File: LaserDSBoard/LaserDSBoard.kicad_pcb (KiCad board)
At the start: 4 copper layers, 139.5 x 77 mm, 728 parts, among them J1 JTAG, J10 D SWITCH, J11 LASER, J12 Y VREF, J13 X VREF, J14 Y1 MOTOR, J15 X MOTOR, J16 Y2 MOTOR, J17 Y VREF, J2 USB, J3 POWER IN, J4 LASER P, J5 X LIMIT1, J6 WATER FLOW, J7 X LIMIT2, J8 Y LIMIT1, J9 Y LIMIT2, SW1 DHT-1163S, SW2 SSSS213202, U1 LD1117S, U10 TLP2355, U11 ADUM1250, U12 TLP2355, U13 TLP2355, U14 TLP2355, U15 TLP2355, U16 TLP2355, U17 TLP2355, U18 TLP2355, U19 MCP3425, U2 LD1117S, U20 A4982SLPTR, U21 A4982SLPTR, U22 TLP2355, U23 TPL0401A, U24 TPL0401B, U25 A4982SLPTR, U3 STM32F20XR, U4 LD1117S, U5 ADUM1250, U6 TLP2355, U7 TLP2355, U8 TLP2355, U9 TLP2355, X1 7B-25.000MAAJ-T, X2 9HT10-32.768KDZY-T

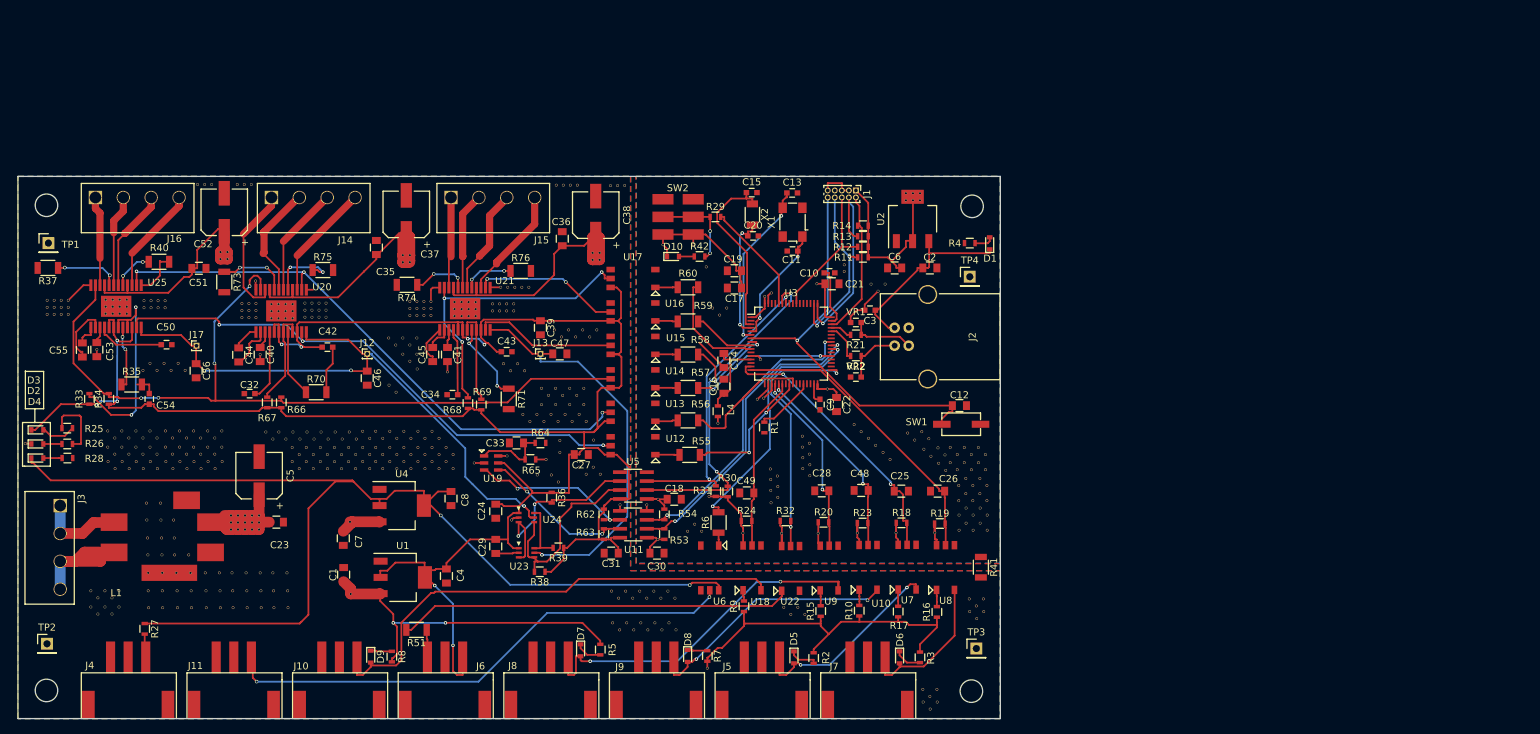
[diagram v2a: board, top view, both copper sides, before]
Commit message: Ver2.0.0
[schematic]
・デジタルポテンショメータ　MCP4461に戻す
・フォトカプラ ENの経路(U14,U17,U29)
TLP2355→TLP291に変更

[AW]
・回路図変更に伴うAW変更
・モータドライバ回りビア増加
・SW2の向きを反転
・部品実装マークをシルクで追加
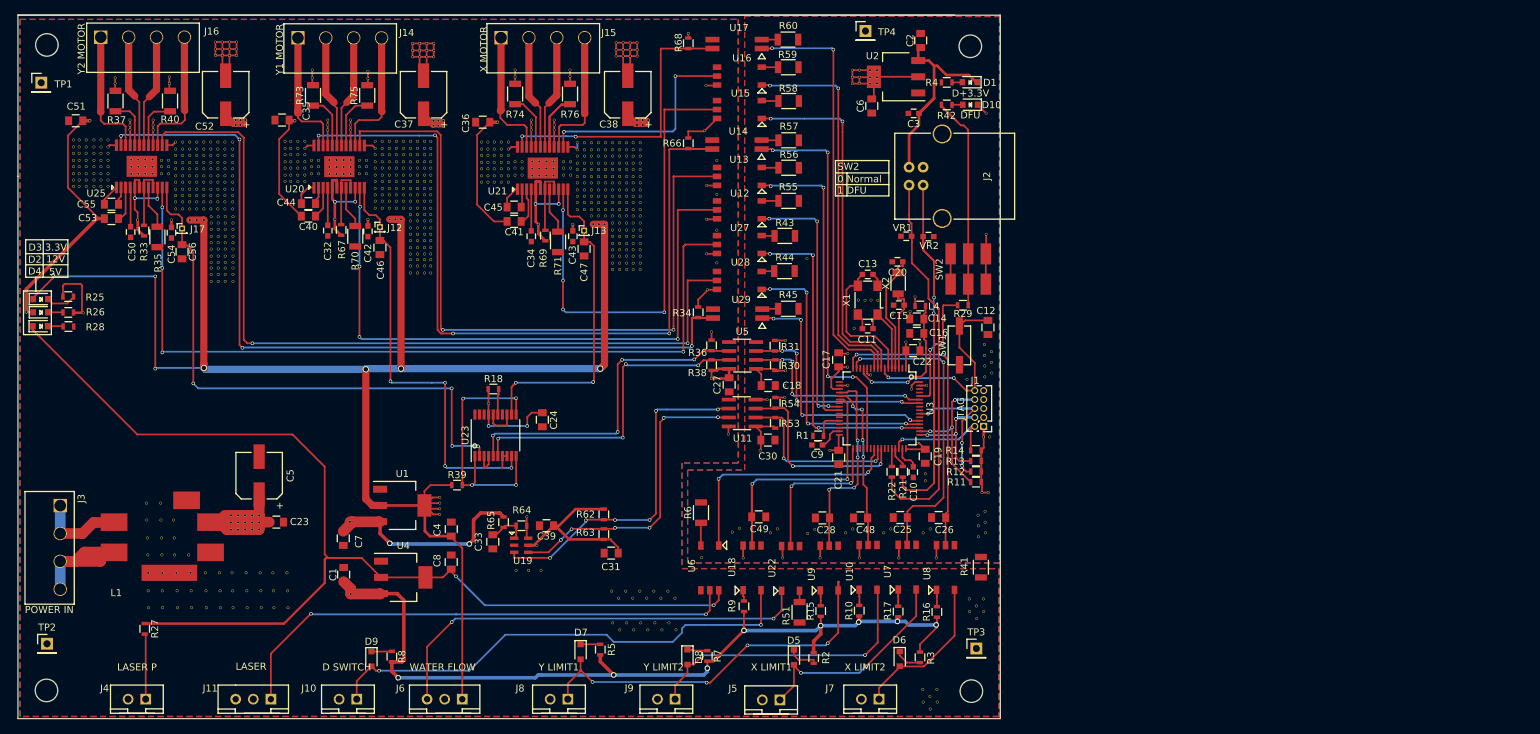
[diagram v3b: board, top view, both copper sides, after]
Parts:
- removed the ? at (201.2, 127.0)
- removed the ? at (243.2, 127.2)
- removed the ? at (244.2, 128.2)
- removed the ? at (244.2, 129.8)
- removed the ? at (243.2, 128.8)
- removed the ? at (243.1, 125.8)
- removed the ? at (244.1, 126.8)
- removed the ? at (254.6, 126.5)
- removed the ? at (255.6, 127.5)
- removed the ? at (253.5, 125.5)
- removed the ? at (252.5, 124.5)
- removed the ? at (250.4, 122.5)
- removed the ? at (251.4, 123.5)
- removed the ? at (266.4, 136.6)
- removed the ? at (268.4, 136.6)
- removed the ? at (265.4, 137.6)
- removed the ? at (267.4, 137.6)
- removed the ? at (269.4, 137.6)
- removed the ? at (269.4, 135.4)
- removed the ? at (267.4, 135.4)
- removed the ? at (265.4, 135.4)
- removed the ? at (268.4, 134.4)
- removed the ? at (266.4, 134.4)
- removed the ? at (266.3, 130.2)
- removed the ? at (268.3, 130.2)
- removed the ? at (265.3, 131.2)
- removed the ? at (267.3, 131.2)
- removed the ? at (269.3, 131.2)
- removed the ? at (269.3, 133.3)
- removed the ? at (267.3, 133.3)
- removed the ? at (265.3, 133.3)
- removed the ? at (268.3, 132.3)
- removed the ? at (266.3, 132.3)
- removed the ? at (261.1, 124.5)
- removed the ? at (260.1, 123.5)
- removed the ? at (230.3, 106.0)
- removed the ? at (232.3, 106.0)
- removed the ? at (231.3, 107.0)
- removed the ? at (228.4, 99.2)
- removed the ? at (229.4, 100.2)
- removed the ? at (224.7, 98.8)
- removed the ? at (226.6, 99.2)
- removed the ? at (224.6, 99.2)
- removed the ? at (237.2, 113.3)
- removed the ? at (263.4, 129.1)
- removed the ? at (262.4, 128.1)
- removed the ? at (227.8, 136.7)
- removed the ? at (226.8, 137.7)
- removed the ? at (264.1, 128.0)
- removed the ? at (266.1, 128.0)
- removed the ? at (268.1, 128.0)
- removed the ? at (265.1, 128.9)
- removed the ? at (267.1, 128.9)
- removed the ? at (269.1, 128.9)
- removed the ? at (249.1, 100.8)
- removed the ? at (249.1, 99.8)
- removed the ? at (252.8, 102.6)
- removed the ? at (254.8, 102.6)
- removed the ? at (253.8, 103.6)
- removed the ? at (238.7, 103.8)
- removed the ? at (193.5, 128.8)
- removed the ? at (191.5, 128.8)
- removed the ? at (189.5, 128.8)
- removed the ? at (187.5, 128.8)
- removed the ? at (185.5, 128.8)
- removed the ? at (183.5, 128.8)
- removed the ? at (192.5, 127.8)
- removed the ? at (190.5, 127.8)
- removed the ? at (188.5, 127.8)
- removed the ? at (186.5, 127.8)
- removed the ? at (184.5, 127.8)
- removed the ? at (182.5, 127.8)
- removed the ? at (170.7, 127.8)
- removed the ? at (172.7, 127.8)
- removed the ? at (174.7, 127.8)
- removed the ? at (176.7, 127.8)
- removed the ? at (178.7, 127.8)
- removed the ? at (180.7, 127.8)
- removed the ? at (171.7, 128.8)
- removed the ? at (173.7, 128.8)
- removed the ? at (175.7, 128.8)
- removed the ? at (177.7, 128.8)
- removed the ? at (179.7, 128.8)
- removed the ? at (181.7, 128.8)
- removed the ? at (168.8, 123.6)
- removed the ? at (170.8, 123.6)
- removed the ? at (172.8, 123.6)
- removed the ? at (174.8, 123.6)
- removed the ? at (176.8, 123.6)
- removed the ? at (178.8, 123.6)
- removed the ? at (169.8, 124.6)
- removed the ? at (171.8, 124.6)
- removed the ? at (173.8, 124.6)
- removed the ? at (175.8, 124.6)
- removed the ? at (177.8, 124.6)
- removed the ? at (179.8, 124.6)
- removed the ? at (167.9, 124.6)
- removed the ? at (166.9, 123.6)
- removed the ? at (213.4, 124.8)
- removed the ? at (208.7, 124.8)
- removed the ? at (208.7, 126.5)
- removed the ? at (208.4, 130.7)
- removed the ? at (201.8, 136.1)
- removed the ? at (207.4, 129.7)
- removed the ? at (205.4, 129.7)
- removed the ? at (211.4, 128.6)
- removed the ? at (213.4, 128.6)
- removed the ? at (212.4, 129.6)
- removed the ? at (214.4, 129.6)
- removed the ? at (203.7, 114.9)
- removed the ? at (201.7, 114.9)
- removed the ? at (202.7, 113.9)
- removed the ? at (200.7, 113.9)
- removed the ? at (207.9, 109.1)
- removed the ? at (209.9, 109.1)
- removed the ? at (211.9, 109.1)
- removed the ? at (213.9, 109.1)
- removed the ? at (208.9, 110.1)
- removed the ? at (210.9, 110.1)
- removed the ? at (212.9, 110.1)
- removed the ? at (212.4, 122.1)
- removed the ? at (210.4, 122.1)
- removed the ? at (208.4, 122.1)
- removed the ? at (206.4, 122.1)
- removed the ? at (204.4, 122.1)
- removed the ? at (211.4, 121.1)
- removed the ? at (209.4, 121.1)
- removed the ? at (207.4, 121.1)
- removed the ? at (205.4, 121.1)
- removed the ? at (203.4, 121.1)
- removed the ? at (206.1, 119.7)
- removed the ? at (208.1, 119.7)
- removed the ? at (210.1, 119.7)
- removed the ? at (212.1, 119.7)
- removed the ? at (211.1, 118.4)
- removed the ? at (209.1, 118.4)
- removed the ? at (207.1, 118.4)
- removed the ? at (212.1, 117.4)
- removed the ? at (210.1, 117.4)
- removed the ? at (208.1, 117.4)
- removed the ? at (206.1, 117.4)
- removed the ? at (144.4, 123.5)
- removed the ? at (146.4, 123.5)
- removed the ? at (148.4, 123.5)
- removed the ? at (150.4, 123.5)
- removed the ? at (145.4, 124.5)
- removed the ? at (147.4, 124.5)
- removed the ? at (149.4, 124.5)
- removed the ? at (151.4, 124.5)
- removed the ? at (151.4, 126.8)
- removed the ? at (149.4, 126.8)
- removed the ? at (145.4, 126.8)
- removed the ? at (150.4, 125.8)
- removed the ? at (148.4, 125.8)
- removed the ? at (144.4, 125.8)
- removed the ? at (142.1, 148.4)
- removed the ? at (144.1, 148.4)
- removed the ? at (146.1, 148.4)
- removed the ? at (143.1, 149.4)
- removed the ? at (145.1, 149.4)
- removed the ? at (145.1, 147.2)
- removed the ? at (143.1, 147.2)
- removed the ? at (146.1, 146.2)
- removed the ? at (144.1, 146.2)
- removed the ? at (142.1, 146.2)
- removed the ? at (156.7, 125.8)
- removed the ? at (158.7, 125.8)
- removed the ? at (199.5, 125.0)
- removed the ? at (160.7, 125.8)
- removed the ? at (153.7, 126.8)
- removed the ? at (157.7, 126.8)
- removed the ? at (159.7, 126.8)
- removed the ? at (159.7, 124.5)
- removed the ? at (157.7, 124.5)
- removed the ? at (155.7, 124.5)
- removed the ? at (153.7, 124.5)
- removed the ? at (160.7, 123.5)
- removed the ? at (158.7, 123.5)
- removed the ? at (156.7, 123.5)
- removed the ? at (154.7, 123.5)
- removed the ? at (152.7, 123.5)
- removed the ? at (184.3, 110.2)
- removed the ? at (186.3, 110.2)
- removed the ? at (188.3, 110.2)
- removed the ? at (185.3, 111.2)
- removed the ? at (187.3, 111.2)
- removed the ? at (187.3, 113.5)
- removed the ? at (188.3, 112.5)
- removed the ? at (186.3, 112.5)
- removed the ? at (184.4, 117.0)
- removed the ? at (185.4, 118.0)
- removed the ? at (188.4, 114.7)
- removed the ? at (180.7, 123.5)
- removed the ? at (181.7, 124.5)
- removed the ? at (181.7, 126.8)
- removed the ? at (179.7, 126.8)
- removed the ? at (177.7, 126.8)
- removed the ? at (175.7, 126.8)
- removed the ? at (173.7, 126.8)
- removed the ? at (171.7, 126.8)
- removed the ? at (180.7, 125.8)
- removed the ? at (178.7, 125.8)
- removed the ? at (176.7, 125.8)
- removed the ? at (174.7, 125.8)
- removed the ? at (172.7, 125.8)
- removed the ? at (170.7, 125.8)
- removed the ? at (182.5, 125.8)
- removed the ? at (184.5, 125.8)
- removed the ? at (186.5, 125.8)
- removed the ? at (188.5, 125.8)
- removed the ? at (190.5, 125.8)
- removed the ? at (192.5, 125.8)
- removed the ? at (183.5, 126.8)
- removed the ? at (185.5, 126.8)
- removed the ? at (187.5, 126.8)
- removed the ? at (189.5, 126.8)
- removed the ? at (191.5, 126.8)
- removed the ? at (193.5, 126.8)
- removed the ? at (151.4, 114.8)
- removed the ? at (191.5, 124.5)
- removed the ? at (189.5, 124.5)
- removed the ? at (187.5, 124.5)
- removed the ? at (185.5, 124.5)
- removed the ? at (183.5, 124.5)
- removed the ? at (155.4, 114.8)
- removed the ? at (153.4, 114.8)
- removed the ? at (149.4, 114.8)
- removed the ? at (190.5, 123.5)
- removed the ? at (188.5, 123.5)
- removed the ? at (186.5, 123.5)
- removed the ? at (184.5, 123.5)
- removed the ? at (182.5, 123.5)
- removed the ? at (154.4, 113.8)
- removed the ? at (152.4, 113.8)
- removed the ? at (150.4, 113.8)
- removed the ? at (246.7, 117.5)
- removed the ? at (245.2, 102.5)
- removed the ? at (229.8, 132.8)
- removed the ? at (222.6, 133.2)
- removed the ? at (261.9, 137.9)
- removed the ? at (250.9, 137.9)
- removed the ? at (237.6, 118.8)
- removed the ? at (231.1, 122.3)
- removed the ? at (237.8, 104.3)
- removed the ? at (227.6, 97.0)
- removed the ? at (223.3, 97.0)
- removed the ? at (222.6, 138.8)
- removed the ? at (256.4, 137.9)
- removed the ? at (245.3, 138.0)
- removed the ? at (240.2, 138.0)
- removed the ? at (234.7, 137.9)
- removed the ? at (221.0, 133.9)
- removed the ? at (236.7, 119.0)
- removed the ? at (269.1, 126.8)
- removed the ? at (267.1, 126.8)
- removed the ? at (265.1, 126.8)
- removed the ? at (268.1, 125.8)
- removed the ? at (266.1, 125.8)
- removed the ? at (187.3, 99.5)
- removed the ? at (186.3, 99.5)
- removed the ? at (214.3, 99.2)
- removed the ? at (213.3, 99.2)
- removed the ? at (161.4, 99.0)
- removed the ? at (160.4, 99.0)
- removed the ? at (187.3, 98.5)
- removed the ? at (186.3, 98.5)
- removed the ? at (214.3, 98.2)
- removed the ? at (213.3, 98.2)
- removed the ? at (142.9, 111.9)
- removed the ? at (166.1, 112.6)
- removed the ? at (192.7, 115.0)
- removed the ? at (161.4, 98.0)
- removed the ? at (160.4, 98.0)
- removed the ? at (206.7, 127.5)
- removed the ? at (190.3, 107.0)
- removed the ? at (189.3, 107.0)
- removed the ? at (188.3, 107.0)
- removed the ? at (187.3, 107.0)
- removed the ? at (175.4, 107.3)
- removed the ? at (174.4, 107.3)
- removed the ? at (173.4, 107.3)
- removed the ? at (172.4, 107.3)
- removed the ? at (165.5, 107.3)
- removed the ? at (164.5, 107.3)
- removed the ? at (163.5, 107.3)
- removed the ? at (204.2, 103.0)
- removed the ? at (203.2, 103.0)
- removed the ? at (202.2, 103.0)
- removed the ? at (201.2, 103.0)
- removed the ? at (200.2, 103.0)
- removed the ? at (190.3, 106.0)
- removed the ? at (189.3, 106.0)
- removed the ? at (188.3, 106.0)
- removed the ? at (187.3, 106.0)
- removed the ? at (175.4, 106.3)
- removed the ? at (174.4, 106.3)
- removed the ? at (173.4, 106.3)
- removed the ? at (172.4, 106.3)
- removed the ? at (165.5, 106.3)
- removed the ? at (164.5, 106.3)
- removed the ? at (163.5, 106.3)
- removed the ? at (190.3, 105.0)
- removed the ? at (189.3, 105.0)
- removed the ? at (188.3, 105.0)
- removed the ? at (187.3, 105.0)
- removed the ? at (175.4, 105.3)
- removed the ? at (174.4, 105.3)
- removed the ? at (173.4, 105.3)
- removed the ? at (172.4, 105.3)
- removed the ? at (165.5, 105.3)
- removed the ? at (164.5, 105.3)
- removed the ? at (163.5, 105.3)
- removed the ? at (138.8, 106.9)
- removed the ? at (137.8, 106.9)
- removed the ? at (136.8, 106.9)
- removed the ? at (135.8, 106.9)
- removed the ? at (152.6, 106.0)
- removed the ? at (151.6, 106.0)
- removed the ? at (150.6, 106.0)
- removed the ? at (149.6, 106.0)
- removed the ? at (138.8, 105.9)
- removed the ? at (137.8, 105.9)
- removed the ? at (136.8, 105.9)
- removed the ? at (135.8, 105.9)
- removed the ? at (243.4, 149.5)
- removed the ? at (152.6, 105.0)
- removed the ? at (241.4, 149.5)
- removed the ? at (151.6, 105.0)
- removed the ? at (150.6, 105.0)
- removed the ? at (149.6, 105.0)
- removed the ? at (138.8, 104.9)
- removed the ? at (137.8, 104.9)
- removed the ? at (136.8, 104.9)
- removed the ? at (135.8, 104.9)
- removed the ? at (242.4, 148.5)
- removed the ? at (240.4, 148.5)
- removed the ? at (159.7, 128.8)
- removed the ? at (157.7, 128.8)
- removed the ? at (155.7, 128.8)
- removed the ? at (153.7, 128.8)
- removed the ? at (160.7, 127.8)
- removed the ? at (158.7, 127.8)
- removed the ? at (156.7, 127.8)
- removed the ? at (152.7, 127.8)
- removed the ? at (144.5, 127.8)
- removed the ? at (146.5, 127.8)
- removed the ? at (148.5, 127.8)
- removed the ? at (150.5, 127.8)
- removed the ? at (145.5, 128.8)
- removed the ? at (147.5, 128.8)
- removed the ? at (149.5, 128.8)
- removed the ? at (151.5, 128.8)
- removed the ? at (165.4, 102.2)
- removed the ? at (217.2, 133.9)
- removed the ? at (262.4, 125.8)
- removed the ? at (263.4, 126.8)
- removed the ? at (261.4, 127.0)
- removed the ? at (260.4, 126.0)
- removed the ? at (258.1, 123.8)
- removed the ? at (259.1, 124.8)
- removed the ? at (159.2, 88.5)
- removed the ? at (158.2, 88.5)
- removed the ? at (157.2, 88.5)
- removed the ? at (162.8, 88.5)
- removed the ? at (163.8, 88.5)
- removed the ? at (164.8, 88.5)
- removed the ? at (217.8, 88.6)
- removed the ? at (216.8, 88.6)
- removed the ? at (215.8, 88.6)
- removed the ? at (208.2, 88.5)
- removed the ? at (209.2, 88.5)
- removed the ? at (210.2, 88.5)
- removed the ? at (211.2, 88.5)
- removed the ? at (238.7, 133.7)
- removed the ? at (239.6, 129.8)
- removed the ? at (238.6, 128.8)
- removed the ? at (238.6, 131.9)
- removed the ? at (239.6, 132.9)
- removed the ? at (239.6, 131.3)
- removed the ? at (238.6, 130.3)
- removed C29: 0u1, Capacitors_SMD:C_0805
- removed R19, R20, R23, R24, R32: 1k, Resistors_SMD:R_0603
- removed U24: TPL0401B, mylib:TPL0401
- added ?: , mylib:via, F.Cu at (266.5, 116.1)
- added ?: , mylib:via, F.Cu at (219.1, 84.4)
- added ?: , mylib:via, F.Cu at (180.2, 86.9)
- added ?: , mylib:via, F.Cu at (181.2, 85.9)
- added ?: , mylib:via, F.Cu at (180.2, 85.9)
- added ?: , mylib:via, F.Cu at (153.1, 85.0)
- added ?: , mylib:via, F.Cu at (152.1, 85.0)
- added ?: , mylib:via, F.Cu at (153.1, 86.9)
- added ?: , mylib:via, F.Cu at (152.1, 86.9)
- added ?: , mylib:via, F.Cu at (153.1, 85.9)
- added ?: , mylib:via, F.Cu at (152.1, 85.9)
- added ?: , mylib:via, F.Cu at (173.4, 85.9)
- added ?: , mylib:via, F.Cu at (220.1, 84.4)
- added ?: , mylib:via, F.Cu at (174.4, 85.9)
- added ?: , mylib:via, F.Cu at (173.4, 86.9)
- added ?: , mylib:via, F.Cu at (174.4, 86.9)
- added ?: , mylib:via, F.Cu at (173.4, 85.0)
- added ?: , mylib:via, F.Cu at (174.4, 85.0)
- added ?: , mylib:via, F.Cu at (144.5, 88.7)
- added ?: , mylib:via, F.Cu at (143.5, 88.7)
- added ?: , mylib:via, F.Cu at (142.5, 88.7)
- added ?: , mylib:via, F.Cu at (140.4, 88.7)
- added ?: , mylib:via, F.Cu at (141.4, 88.7)
- added ?: , mylib:via, F.Cu at (219.1, 85.4)
- added ?: , mylib:via, F.Cu at (139.6, 88.7)
- added ?: , mylib:via, F.Cu at (139.6, 82.1)
- added ?: , mylib:via, F.Cu at (139.6, 83.1)
- added ?: , mylib:via, F.Cu at (139.6, 85.0)
- added ?: , mylib:via, F.Cu at (139.6, 84.0)
- added ?: , mylib:via, F.Cu at (139.6, 87.8)
- added ?: , mylib:via, F.Cu at (139.6, 86.9)
- added ?: , mylib:via, F.Cu at (139.6, 85.9)
- added ?: , mylib:via, F.Cu at (140.4, 85.9)
- added ?: , mylib:via, F.Cu at (141.4, 85.9)
- added ?: , mylib:via, F.Cu at (220.1, 85.4)
- added ?: , mylib:via, F.Cu at (140.4, 86.9)
- added ?: , mylib:via, F.Cu at (141.4, 86.9)
- added ?: , mylib:via, F.Cu at (141.4, 87.8)
- added ?: , mylib:via, F.Cu at (140.4, 87.8)
- added ?: , mylib:via, F.Cu at (140.4, 84.0)
- added ?: , mylib:via, F.Cu at (141.4, 84.0)
- added ?: , mylib:via, F.Cu at (140.4, 85.0)
- added ?: , mylib:via, F.Cu at (141.4, 85.0)
- added ?: , mylib:via, F.Cu at (141.4, 83.1)
- added ?: , mylib:via, F.Cu at (140.4, 83.1)
- added ?: , mylib:via, F.Cu at (220.1, 83.5)
- added ?: , mylib:via, F.Cu at (141.4, 82.1)
- added ?: , mylib:via, F.Cu at (140.4, 82.1)
- added ?: , mylib:via, F.Cu at (210.1, 73.1)
- added ?: , mylib:via, F.Cu at (210.1, 72.2)
- added ?: , mylib:via, F.Cu at (202.3, 72.2)
- added ?: , mylib:via, F.Cu at (202.3, 73.2)
- added ?: , mylib:via, F.Cu at (181.4, 73.4)
- added ?: , mylib:via, F.Cu at (181.4, 72.4)
- added ?: , mylib:via, F.Cu at (173.5, 72.2)
- added ?: , mylib:via, F.Cu at (173.5, 73.3)
- added ?: , mylib:via, F.Cu at (219.1, 83.5)
- added ?: , mylib:via, F.Cu at (153.2, 74.1)
- added ?: , mylib:via, F.Cu at (153.2, 73.2)
- added ?: , mylib:via, F.Cu at (145.5, 73.3)
- added ?: , mylib:via, F.Cu at (145.5, 74.1)
- added ?: , mylib:via, F.Cu at (159.7, 70.1)
- added ?: , mylib:via, F.Cu at (160.7, 70.1)
- added ?: , mylib:via, F.Cu at (161.7, 70.1)
- added ?: , mylib:via, F.Cu at (162.7, 70.1)
- added ?: , mylib:via, F.Cu at (162.7, 69.2)
- added ?: , mylib:via, F.Cu at (161.7, 69.2)
- added ?: , mylib:via, F.Cu at (220.1, 82.5)
- added ?: , mylib:via, F.Cu at (160.7, 69.2)
- added ?: , mylib:via, F.Cu at (159.7, 69.2)
- added ?: , mylib:via, F.Cu at (162.7, 68.2)
- added ?: , mylib:via, F.Cu at (161.7, 68.2)
- added ?: , mylib:via, F.Cu at (160.7, 68.2)
- added ?: , mylib:via, F.Cu at (159.7, 68.2)
- added ?: , mylib:via, F.Cu at (187.7, 68.4)
- added ?: , mylib:via, F.Cu at (188.7, 68.4)
- added ?: , mylib:via, F.Cu at (189.7, 68.4)
- added ?: , mylib:via, F.Cu at (190.7, 68.4)
- added ?: , mylib:via, F.Cu at (219.1, 82.5)
- added ?: , mylib:via, F.Cu at (187.7, 69.4)
- added ?: , mylib:via, F.Cu at (188.7, 69.4)
- added ?: , mylib:via, F.Cu at (189.7, 69.4)
- added ?: , mylib:via, F.Cu at (190.7, 69.4)
- added ?: , mylib:via, F.Cu at (190.7, 70.3)
- added ?: , mylib:via, F.Cu at (189.7, 70.3)
- added ?: , mylib:via, F.Cu at (188.7, 70.3)
- added ?: , mylib:via, F.Cu at (187.7, 70.3)
- added ?: , mylib:via, F.Cu at (216.6, 70.2)
- added ?: , mylib:via, F.Cu at (217.6, 70.2)
- added ?: , mylib:via, F.Cu at (219.1, 91.0)
- added ?: , mylib:via, F.Cu at (218.6, 70.2)
- added ?: , mylib:via, F.Cu at (219.6, 70.2)
- added ?: , mylib:via, F.Cu at (219.6, 69.3)
- added ?: , mylib:via, F.Cu at (218.6, 69.3)
- added ?: , mylib:via, F.Cu at (217.6, 69.3)
- added ?: , mylib:via, F.Cu at (216.6, 69.3)
- added ?: , mylib:via, F.Cu at (219.6, 68.3)
- added ?: , mylib:via, F.Cu at (218.6, 68.3)
- added ?: , mylib:via, F.Cu at (217.6, 68.3)
- added ?: , mylib:via, F.Cu at (216.6, 68.3)
- added ?: , mylib:via, F.Cu at (220.1, 91.0)
- added ?: , mylib:via, F.Cu at (182.4, 85.2)
- added ?: , mylib:via, F.Cu at (240.6, 117.0)
- added ?: , mylib:via, F.Cu at (240.6, 118.7)
- added ?: , mylib:via, F.Cu at (234.2, 137.3)
- added ?: , mylib:via, F.Cu at (233.2, 137.8)
- added ?: , mylib:via, F.Cu at (238.6, 137.9)
- added ?: , mylib:via, F.Cu at (239.6, 137.4)
- added ?: , mylib:via, F.Cu at (244.8, 137.5)
- added ?: , mylib:via, F.Cu at (243.8, 138.0)
- added ?: , mylib:via, F.Cu at (249.2, 137.9)
- added ?: , mylib:via, F.Cu at (219.1, 86.3)
- added ?: , mylib:via, F.Cu at (219.1, 92.0)
- added ?: , mylib:via, F.Cu at (250.2, 137.4)
- added ?: , mylib:via, F.Cu at (254.7, 137.9)
- added ?: , mylib:via, F.Cu at (255.7, 137.4)
- added ?: , mylib:via, F.Cu at (261.2, 137.4)
- added ?: , mylib:via, F.Cu at (260.2, 137.9)
- added ?: , mylib:via, F.Cu at (268.1, 136.9)
- added ?: , mylib:via, F.Cu at (269.1, 137.9)
- added ?: , mylib:via, F.Cu at (268.1, 138.5)
- added ?: , mylib:via, F.Cu at (268.1, 135.4)
- added ?: , mylib:via, F.Cu at (269.1, 136.4)
- added ?: , mylib:via, F.Cu at (220.1, 92.0)
- added ?: , mylib:via, F.Cu at (269.1, 134.9)
- added ?: , mylib:via, F.Cu at (259.4, 125.2)
- added ?: , mylib:via, F.Cu at (237.1, 126.2)
- added ?: , mylib:via, F.Cu at (247.0, 126.2)
- added ?: , mylib:via, F.Cu at (249.5, 114.4)
- added ?: , mylib:via, F.Cu at (249.6, 117.0)
- added ?: , mylib:via, F.Cu at (257.8, 110.8)
- added ?: , mylib:via, F.Cu at (260.8, 117.0)
- added ?: , mylib:via, F.Cu at (252.8, 115.5)
- added ?: , mylib:via, F.Cu at (249.6, 112.5)
- added ?: , mylib:via, F.Cu at (220.1, 90.1)
- added ?: , mylib:via, F.Cu at (250.4, 108.9)
- added ?: , mylib:via, F.Cu at (259.8, 110.8)
- added ?: , mylib:via, F.Cu at (258.6, 117.5)
- added ?: , mylib:via, F.Cu at (259.1, 104.4)
- added ?: , mylib:via, F.Cu at (255.9, 106.9)
- added ?: , mylib:via, F.Cu at (258.4, 106.5)
- added ?: , mylib:via, F.Cu at (252.8, 104.9)
- added ?: , mylib:via, F.Cu at (253.8, 104.9)
- added ?: , mylib:via, F.Cu at (268.6, 132.2)
- added ?: , mylib:via, F.Cu at (269.5, 132.2)
- added ?: , mylib:via, F.Cu at (219.1, 90.1)
- added ?: , mylib:via, F.Cu at (269.7, 124.3)
- added ?: , mylib:via, F.Cu at (268.9, 111.2)
- added ?: , mylib:via, F.Cu at (269.9, 112.2)
- added ?: , mylib:via, F.Cu at (269.9, 113.7)
- added ?: , mylib:via, F.Cu at (268.9, 112.7)
- added ?: , mylib:via, F.Cu at (269.0, 115.8)
- added ?: , mylib:via, F.Cu at (270.0, 115.2)
- added ?: , mylib:via, F.Cu at (269.0, 114.2)
- added ?: , mylib:via, F.Cu at (269.2, 95.5)
- added ?: , mylib:via, F.Cu at (252.7, 72.2)
- added ?: , mylib:via, F.Cu at (219.1, 92.9)
- added ?: , mylib:via, F.Cu at (253.7, 72.2)
- added ?: , mylib:via, F.Cu at (253.7, 74.1)
- added ?: , mylib:via, F.Cu at (252.7, 73.2)
- added ?: , mylib:via, F.Cu at (253.7, 73.2)
- added ?: , mylib:via, F.Cu at (252.7, 74.1)
- added ?: , mylib:via, F.Cu at (250.2, 74.1)
- added ?: , mylib:via, F.Cu at (240.7, 110.6)
- added ?: , mylib:via, F.Cu at (240.7, 114.9)
- added ?: , mylib:via, F.Cu at (232.6, 123.9)
- added ?: , mylib:via, F.Cu at (230.2, 116.0)
- added ?: , mylib:via, F.Cu at (220.1, 92.9)
- added ?: , mylib:via, F.Cu at (230.2, 109.4)
- added ?: , mylib:via, F.Cu at (205.4, 139.7)
- added ?: , mylib:via, F.Cu at (226.9, 67.0)
- added ?: , mylib:via, F.Cu at (229.2, 80.8)
- added ?: , mylib:via, F.Cu at (229.4, 74.4)
- added ?: , mylib:via, F.Cu at (229.5, 88.6)
- added ?: , mylib:via, F.Cu at (229.5, 93.4)
- added ?: , mylib:via, F.Cu at (229.6, 103.4)
- added ?: , mylib:via, F.Cu at (229.5, 98.3)
- added ?: , mylib:via, F.Cu at (191.6, 134.5)
- added ?: , mylib:via, F.Cu at (220.1, 100.5)
- added ?: , mylib:via, F.Cu at (191.6, 135.3)
- added ?: , mylib:via, F.Cu at (191.6, 133.7)
- added ?: , mylib:via, F.Cu at (171.0, 79.4)
- added ?: , mylib:via, F.Cu at (141.9, 79.4)
- added ?: , mylib:via, F.Cu at (147.6, 79.3)
- added ?: , mylib:via, F.Cu at (189.4, 91.8)
- added ?: , mylib:via, F.Cu at (188.4, 91.8)
- added ?: , mylib:via, F.Cu at (187.4, 91.8)
- added ?: , mylib:via, F.Cu at (187.4, 92.7)
- added ?: , mylib:via, F.Cu at (188.4, 92.7)
- added ?: , mylib:via, F.Cu at (219.1, 100.5)
- added ?: , mylib:via, F.Cu at (189.4, 92.7)
- added ?: , mylib:via, F.Cu at (189.4, 94.6)
- added ?: , mylib:via, F.Cu at (188.4, 94.6)
- added ?: , mylib:via, F.Cu at (187.4, 94.6)
- added ?: , mylib:via, F.Cu at (189.4, 93.6)
- added ?: , mylib:via, F.Cu at (188.4, 93.6)
- added ?: , mylib:via, F.Cu at (187.4, 93.6)
- added ?: , mylib:via, F.Cu at (187.4, 96.4)
- added ?: , mylib:via, F.Cu at (188.4, 96.4)
- added ?: , mylib:via, F.Cu at (189.4, 96.4)
- added ?: , mylib:via, F.Cu at (219.1, 97.7)
- added ?: , mylib:via, F.Cu at (187.4, 97.4)
- added ?: , mylib:via, F.Cu at (188.4, 97.4)
- added ?: , mylib:via, F.Cu at (189.4, 97.4)
- added ?: , mylib:via, F.Cu at (189.4, 95.5)
- added ?: , mylib:via, F.Cu at (188.4, 95.5)
- added ?: , mylib:via, F.Cu at (187.4, 95.5)
- added ?: , mylib:via, F.Cu at (187.4, 98.3)
- added ?: , mylib:via, F.Cu at (188.4, 98.3)
- added ?: , mylib:via, F.Cu at (189.4, 98.3)
- added ?: , mylib:via, F.Cu at (187.4, 99.1)
- added ?: , mylib:via, F.Cu at (220.1, 97.7)
- added ?: , mylib:via, F.Cu at (188.4, 99.1)
- added ?: , mylib:via, F.Cu at (189.4, 99.1)
- added ?: , mylib:via, F.Cu at (189.4, 101.0)
- added ?: , mylib:via, F.Cu at (188.4, 101.0)
- added ?: , mylib:via, F.Cu at (187.4, 101.0)
- added ?: , mylib:via, F.Cu at (189.4, 100.0)
- added ?: , mylib:via, F.Cu at (188.4, 100.0)
- added ?: , mylib:via, F.Cu at (187.4, 100.0)
- added ?: , mylib:via, F.Cu at (162.2, 100.3)
- added ?: , mylib:via, F.Cu at (162.2, 102.2)
- added ?: , mylib:via, F.Cu at (220.1, 86.3)
- added ?: , mylib:via, F.Cu at (220.1, 99.6)
- added ?: , mylib:via, F.Cu at (162.2, 101.2)
- added ?: , mylib:via, F.Cu at (159.1, 101.2)
- added ?: , mylib:via, F.Cu at (160.1, 101.2)
- added ?: , mylib:via, F.Cu at (161.1, 101.2)
- added ?: , mylib:via, F.Cu at (159.1, 102.2)
- added ?: , mylib:via, F.Cu at (160.1, 102.2)
- added ?: , mylib:via, F.Cu at (161.1, 102.2)
- added ?: , mylib:via, F.Cu at (161.1, 100.3)
- added ?: , mylib:via, F.Cu at (160.1, 100.3)
- added ?: , mylib:via, F.Cu at (159.1, 100.3)
- added ?: , mylib:via, F.Cu at (219.1, 99.6)
- added ?: , mylib:via, F.Cu at (162.2, 99.5)
- added ?: , mylib:via, F.Cu at (161.1, 99.5)
- added ?: , mylib:via, F.Cu at (160.1, 99.5)
- added ?: , mylib:via, F.Cu at (159.1, 99.5)
- added ?: , mylib:via, F.Cu at (159.1, 96.7)
- added ?: , mylib:via, F.Cu at (160.1, 96.7)
- added ?: , mylib:via, F.Cu at (161.1, 96.7)
- added ?: , mylib:via, F.Cu at (161.1, 98.6)
- added ?: , mylib:via, F.Cu at (160.1, 98.6)
- added ?: , mylib:via, F.Cu at (159.1, 98.6)
- added ?: , mylib:via, F.Cu at (220.1, 98.6)
- added ?: , mylib:via, F.Cu at (161.1, 97.6)
- added ?: , mylib:via, F.Cu at (160.1, 97.6)
- added ?: , mylib:via, F.Cu at (159.1, 97.6)
- added ?: , mylib:via, F.Cu at (162.2, 97.6)
- added ?: , mylib:via, F.Cu at (162.2, 98.6)
- added ?: , mylib:via, F.Cu at (162.2, 96.7)
- added ?: , mylib:via, F.Cu at (162.2, 93.9)
- added ?: , mylib:via, F.Cu at (162.2, 95.8)
- added ?: , mylib:via, F.Cu at (162.2, 94.8)
- added ?: , mylib:via, F.Cu at (159.1, 94.8)
- added ?: , mylib:via, F.Cu at (219.1, 98.6)
- added ?: , mylib:via, F.Cu at (160.1, 94.8)
- added ?: , mylib:via, F.Cu at (161.1, 94.8)
- added ?: , mylib:via, F.Cu at (159.1, 95.8)
- added ?: , mylib:via, F.Cu at (160.1, 95.8)
- added ?: , mylib:via, F.Cu at (161.1, 95.8)
- added ?: , mylib:via, F.Cu at (161.1, 93.9)
- added ?: , mylib:via, F.Cu at (160.1, 93.9)
- added ?: , mylib:via, F.Cu at (159.1, 93.9)
- added ?: , mylib:via, F.Cu at (216.1, 93.9)
- added ?: , mylib:via, F.Cu at (217.1, 93.9)
- added ?: , mylib:via, F.Cu at (219.1, 95.8)
- added ?: , mylib:via, F.Cu at (218.1, 93.9)
- added ?: , mylib:via, F.Cu at (216.1, 94.9)
- added ?: , mylib:via, F.Cu at (217.1, 94.9)
- added ?: , mylib:via, F.Cu at (218.1, 94.9)
- added ?: , mylib:via, F.Cu at (218.1, 96.8)
- added ?: , mylib:via, F.Cu at (217.1, 96.8)
- added ?: , mylib:via, F.Cu at (216.1, 96.8)
- added ?: , mylib:via, F.Cu at (218.1, 95.8)
- added ?: , mylib:via, F.Cu at (217.1, 95.8)
- added ?: , mylib:via, F.Cu at (216.1, 95.8)
- added ?: , mylib:via, F.Cu at (220.1, 95.8)
- added ?: , mylib:via, F.Cu at (216.1, 98.6)
- added ?: , mylib:via, F.Cu at (217.1, 98.6)
- added ?: , mylib:via, F.Cu at (218.1, 98.6)
- added ?: , mylib:via, F.Cu at (216.1, 99.6)
- added ?: , mylib:via, F.Cu at (217.1, 99.6)
- added ?: , mylib:via, F.Cu at (218.1, 99.6)
- added ?: , mylib:via, F.Cu at (218.1, 97.7)
- added ?: , mylib:via, F.Cu at (217.1, 97.7)
- added ?: , mylib:via, F.Cu at (216.1, 97.7)
- added ?: , mylib:via, F.Cu at (216.1, 100.5)
- added ?: , mylib:via, F.Cu at (219.1, 96.8)
- added ?: , mylib:via, F.Cu at (217.1, 100.5)
- added ?: , mylib:via, F.Cu at (218.1, 100.5)
- added ?: , mylib:via, F.Cu at (162.6, 80.0)
- added ?: , mylib:via, F.Cu at (162.6, 79.3)
- added ?: , mylib:via, F.Cu at (163.3, 79.3)
- added ?: , mylib:via, F.Cu at (163.3, 80.0)
- added ?: , mylib:via, F.Cu at (164.0, 80.0)
- added ?: , mylib:via, F.Cu at (164.0, 79.3)
- added ?: , mylib:via, F.Cu at (220.4, 80.0)
- added ?: , mylib:via, F.Cu at (220.4, 79.3)
- added ?: , mylib:via, F.Cu at (220.1, 96.8)
- added ?: , mylib:via, F.Cu at (192.1, 79.4)
- added ?: , mylib:via, F.Cu at (192.1, 80.1)
- added ?: , mylib:via, F.Cu at (191.4, 80.1)
- added ?: , mylib:via, F.Cu at (191.4, 79.4)
- added ?: , mylib:via, F.Cu at (207.8, 80.0)
- added ?: , mylib:via, F.Cu at (207.8, 79.3)
- added ?: , mylib:via, F.Cu at (207.8, 80.7)
- added ?: , mylib:via, F.Cu at (221.2, 80.0)
- added ?: , mylib:via, F.Cu at (221.2, 79.3)
- added ?: , mylib:via, F.Cu at (190.7, 79.4)
- added ?: , mylib:via, F.Cu at (220.1, 94.9)
- added ?: , mylib:via, F.Cu at (190.7, 80.1)
- added ?: , mylib:via, F.Cu at (204.6, 80.7)
- added ?: , mylib:via, F.Cu at (204.6, 79.3)
- added ?: , mylib:via, F.Cu at (204.6, 80.0)
- added ?: , mylib:via, F.Cu at (219.6, 80.0)
- added ?: , mylib:via, F.Cu at (219.6, 79.3)
- added ?: , mylib:via, F.Cu at (178.9, 80.7)
- added ?: , mylib:via, F.Cu at (178.9, 79.3)
- added ?: , mylib:via, F.Cu at (178.9, 80.0)
- added ?: , mylib:via, F.Cu at (175.7, 80.0)
- added ?: , mylib:via, F.Cu at (219.1, 94.9)
- added ?: , mylib:via, F.Cu at (175.7, 79.3)
- added ?: , mylib:via, F.Cu at (175.7, 80.7)
- added ?: , mylib:via, F.Cu at (150.9, 80.0)
- added ?: , mylib:via, F.Cu at (150.9, 79.3)
- added ?: , mylib:via, F.Cu at (150.9, 80.7)
- added ?: , mylib:via, F.Cu at (147.6, 80.7)
- added ?: , mylib:via, F.Cu at (199.8, 79.6)
- added ?: , mylib:via, F.Cu at (147.6, 80.0)
- added ?: , mylib:via, F.Cu at (148.7, 93.5)
- added ?: , mylib:via, F.Cu at (153.5, 93.5)
- added ?: , mylib:via, F.Cu at (219.1, 87.3)
- added ?: , mylib:via, F.Cu at (220.1, 93.9)
- added ?: , mylib:via, F.Cu at (156.1, 93.5)
- added ?: , mylib:via, F.Cu at (158.1, 93.5)
- added ?: , mylib:via, F.Cu at (157.1, 93.5)
- added ?: , mylib:via, F.Cu at (215.0, 94.1)
- added ?: , mylib:via, F.Cu at (214.2, 94.1)
- added ?: , mylib:via, F.Cu at (213.4, 94.1)
- added ?: , mylib:via, F.Cu at (210.5, 94.1)
- added ?: , mylib:via, F.Cu at (205.6, 94.1)
- added ?: , mylib:via, F.Cu at (176.7, 93.4)
- added ?: , mylib:via, F.Cu at (181.4, 93.4)
- added ?: , mylib:via, F.Cu at (219.1, 93.9)
- added ?: , mylib:via, F.Cu at (184.5, 93.4)
- added ?: , mylib:via, F.Cu at (185.3, 93.4)
- added ?: , mylib:via, F.Cu at (186.1, 93.4)
- added ?: , mylib:via, F.Cu at (142.5, 82.1)
- added ?: , mylib:via, F.Cu at (143.5, 82.1)
- added ?: , mylib:via, F.Cu at (144.5, 82.1)
- added ?: , mylib:via, F.Cu at (142.5, 83.1)
- added ?: , mylib:via, F.Cu at (143.5, 83.1)
- added ?: , mylib:via, F.Cu at (144.5, 83.1)
- added ?: , mylib:via, F.Cu at (144.5, 85.0)
- added ?: , mylib:via, F.Cu at (190.3, 89.9)
- added ?: , mylib:via, F.Cu at (143.5, 85.0)
- added ?: , mylib:via, F.Cu at (142.5, 85.0)
- added ?: , mylib:via, F.Cu at (144.5, 84.0)
- added ?: , mylib:via, F.Cu at (143.5, 84.0)
- added ?: , mylib:via, F.Cu at (142.5, 84.0)
- added ?: , mylib:via, F.Cu at (142.5, 87.8)
- added ?: , mylib:via, F.Cu at (143.5, 87.8)
- added ?: , mylib:via, F.Cu at (144.5, 87.8)
- added ?: , mylib:via, F.Cu at (144.5, 86.9)
- added ?: , mylib:via, F.Cu at (143.5, 86.9)
- added ?: , mylib:via, F.Cu at (190.3, 90.8)
- added ?: , mylib:via, F.Cu at (142.5, 86.9)
- added ?: , mylib:via, F.Cu at (144.5, 85.9)
- added ?: , mylib:via, F.Cu at (143.5, 85.9)
- added ?: , mylib:via, F.Cu at (142.5, 85.9)
- added ?: , mylib:via, F.Cu at (154.1, 90.9)
- added ?: , mylib:via, F.Cu at (155.1, 90.9)
- added ?: , mylib:via, F.Cu at (156.1, 90.9)
- added ?: , mylib:via, F.Cu at (157.1, 90.9)
- added ?: , mylib:via, F.Cu at (154.1, 91.9)
- added ?: , mylib:via, F.Cu at (155.1, 91.9)
- added ?: , mylib:via, F.Cu at (190.3, 82.3)
- added ?: , mylib:via, F.Cu at (156.1, 91.9)
- added ?: , mylib:via, F.Cu at (157.1, 91.9)
- added ?: , mylib:via, F.Cu at (157.1, 90.0)
- added ?: , mylib:via, F.Cu at (156.1, 90.0)
- added ?: , mylib:via, F.Cu at (155.1, 90.0)
- added ?: , mylib:via, F.Cu at (154.1, 90.0)
- added ?: , mylib:via, F.Cu at (158.1, 90.0)
- added ?: , mylib:via, F.Cu at (159.1, 90.0)
- added ?: , mylib:via, F.Cu at (160.1, 90.0)
- added ?: , mylib:via, F.Cu at (161.1, 90.0)
- added ?: , mylib:via, F.Cu at (190.3, 83.3)
- added ?: , mylib:via, F.Cu at (161.1, 91.9)
- added ?: , mylib:via, F.Cu at (160.1, 91.9)
- added ?: , mylib:via, F.Cu at (159.1, 91.9)
- added ?: , mylib:via, F.Cu at (158.1, 91.9)
- added ?: , mylib:via, F.Cu at (161.1, 90.9)
- added ?: , mylib:via, F.Cu at (160.1, 90.9)
- added ?: , mylib:via, F.Cu at (159.1, 90.9)
- added ?: , mylib:via, F.Cu at (158.1, 90.9)
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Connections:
- ? pad 1: GNDA -> A+3.3V
- C24 pad 1: A+3.3V -> GNDA
- C24 pad 2: GNDA -> A+3.3V
- C46 pad 1: Y_REF -> Y1_REF
- C56 pad 1: Y_REF -> Y2_REF
- J12 pad 1: Y_REF -> Y1_REF
- J17 pad 1: Y_REF -> Y2_REF
- R18 pad 1: D+3.3V -> A+3.3V
- R18 pad 2: X_LIMIT1 -> Net-(R18-Pad2)
- R34 pad 2: Y_EN_A -> Y2_EN_A
- R51 pad 1: Net-(J6-Pad3) -> GNDA
- R55 pad 2: Y_STEP -> GNDD
- R56 pad 2: Y_DIR -> GNDD
- R57 pad 2: Y_EN -> GNDD
- R58 pad 2: X_STEP -> GNDD
- R59 pad 2: X_DIR -> GNDD
- R6 pad 2: LASER_OUT -> GNDD
- R60 pad 2: X_EN -> GNDD
- R66 pad 2: Y_EN_A -> Y1_EN_A
- U12 pad 1: Net-(R55-Pad1) -> Y1_STEP
- U12 pad 3: GNDD -> Net-(R55-Pad1)
- U12 pad 5: Y_STEP_A -> Y1_STEP_A
- U13 pad 1: Net-(R56-Pad1) -> Y1_DIR
- U13 pad 3: GNDD -> Net-(R56-Pad1)
- U13 pad 5: Y_DIR_A -> Y1_DIR_A
- U14 pad 1: Net-(R57-Pad1) -> Y1_EN
- U14 pad 3: GNDD -> GNDA
- U14 pad 4: GNDA -> Y1_EN_A
- U15 pad 1: Net-(R58-Pad1) -> X_STEP
- U15 pad 3: GNDD -> Net-(R58-Pad1)
- U16 pad 1: Net-(R59-Pad1) -> X_DIR
- U16 pad 3: GNDD -> Net-(R59-Pad1)
- U17 pad 1: Net-(R60-Pad1) -> X_EN
- U17 pad 3: GNDD -> GNDA
- U17 pad 4: GNDA -> Net-(R68-Pad2)
- U20 pad 11: Y_STEP_A -> Y1_STEP_A
- U20 pad 12: Y_REF -> Y1_REF
- U20 pad 14: Y_DIR_A -> Y1_DIR_A
- U20 pad 23: Y_EN_A -> Y1_EN_A
- U22 pad 1: Net-(R51-Pad2) -> Net-(J6-Pad3)
- U22 pad 3: GNDA -> Net-(R51-Pad2)
- U23 pad 1: A+3.3V -> Net-(R39-Pad2)
- U23 pad 2: GNDA -> Y2_REF
- U23 pad 3: Net-(R36-Pad2) -> GNDA
- U23 pad 4: Net-(R38-Pad2) -> GNDA
- U23 pad 5: X_REF -> Net-(R36-Pad2)
- U23 pad 6: Net-(R39-Pad2) -> Net-(R38-Pad2)
- U25 pad 11: Y_STEP_A -> Y2_STEP_A
- U25 pad 12: Y_REF -> Y2_REF
- U25 pad 14: Y_DIR_A -> Y2_DIR_A
- U25 pad 23: Y_EN_A -> Y2_EN_A
- U3 pad 24: Y_STEP -> Y1_STEP
- U3 pad 25: Y_DIR -> Y1_DIR
- U3 pad 37: Y_EN -> Y1_EN
- U3 pad 51: (no net) -> Y2_STEP
- U3 pad 52: (no net) -> Y2_DIR
- U3 pad 53: (no net) -> Y2_EN
- U6 pad 1: Net-(R6-Pad1) -> LASER_OUT
- U6 pad 3: GNDD -> Net-(R6-Pad1)
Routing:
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- added copper zone on In2.Cu, net A+3.3V
- added copper zone on In2.Cu, net GNDA
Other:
- board size 139.5 x 77 mm -> 139.5 x 99.9 mm
- board text added: "0 Normal 1 DFU"
- board text added: "D+3.3V"
- board text added: "DFU"
- board text added: "SW2"

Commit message: Ver2.0.1
・WATER FLOW　電源をA+3.3V→A+5.0Vにつなぎ変え
・R51 抵抗値変更
220Ω→160Ω
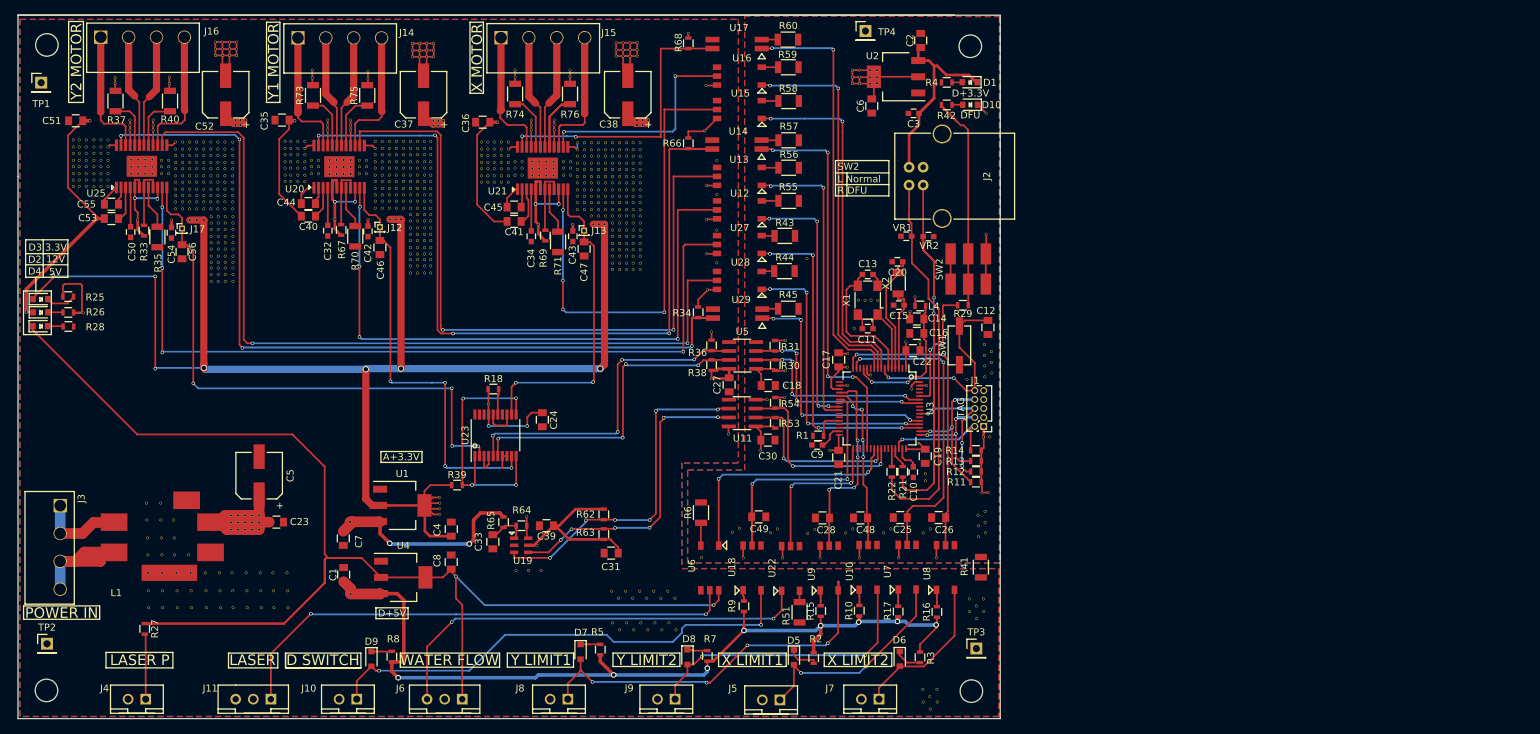
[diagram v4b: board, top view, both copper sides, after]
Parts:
- R51: value 220R -> 160R
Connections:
- J6 pad 1: A+3.3V -> A+5V
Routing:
- net A+3.3V: track 364.0 -> 340.3 mm
- net A+5V: track 195.5 -> 213.3 mm
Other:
- board text added: "A+3.3V"
- board text added: "D+5V"
- board text added: "L Normal R DFU"
- board text added: "Ver 2.0.1"
- board text removed: "0 Normal 1 DFU"
